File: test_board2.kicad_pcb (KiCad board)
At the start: 2 copper layers, 63.5 x 127 mm, 139 parts, among them P1 MicroB, P2 CONN_01X08, P3 CONN_01X08, P4 CONN_01X10, P5 CONN_01X06, P6 CONN_02X03, Q1 ZXMN2F30FHCT-ND, Q2 Si2305DS, SW1 SWITCH_DPDT, SW2 SW_PUSH, SW3 SW_PUSH, SW4 SW_PUSH, SW5 SW_DIP_8, U1 SM220, U2 AS1115, U3 FT230XS, U4 LD1117S33CTR, U5 LIS3DH, U6 TPS61070, U7 NLSX4373

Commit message: Backup
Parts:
- added ?: MountingHole_3mm, Mounting_Holes:MountingHole_3mm, F.Cu at (203.7, 34.0)
- added ?: MountingHole_3mm, Mounting_Holes:MountingHole_3mm, F.Cu at (146.8, 34.0)
- added ?: MountingHole_3mm, Mounting_Holes:MountingHole_3mm, F.Cu at (175.3, 129.5)
- moved D72 134.4 mm to (179.8, 81.3), turned to 180 degrees
- moved D75 131.8 mm to (179.8, 73.7), turned to 180 degrees
- moved D71 128.5 mm to (179.8, 83.8), turned to 180 degrees
- moved D74 125.7 mm to (179.8, 76.2), turned to 180 degrees
- moved D70 122.8 mm to (179.8, 86.4), turned to 180 degrees
- moved D2 121.7 mm to (179.8, 91.4), turned to 180 degrees
- moved D73 119.7 mm to (179.8, 78.7), turned to 180 degrees
- moved D69 117.3 mm to (179.8, 88.9), turned to 180 degrees
- moved R3 56.5 mm to (162.8, 127.8)
- moved R2 54.3 mm to (163.1, 134.6)
- moved C11 50.6 mm to (156.2, 126.5), turned to 180 degrees
- moved C15 50.6 mm to (163.1, 132.3)
- moved C12 49.7 mm to (156.2, 128.5), turned to 180 degrees
- moved Q2 46.9 mm to (156.5, 122.9), turned to 180 degrees
- moved R5 45.1 mm to (166.1, 139.2), turned to 180 degrees
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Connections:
- C11 pad 1: /VREG_IN -> /VIN_USB
- C12 pad 1: /VREG_IN -> /VIN_USB
- SW5 pad 1: Net-(SW5-Pad1) -> Net-(D75-Pad1)
- SW5 pad 10: Net-(D69-Pad1) -> Net-(SW5-Pad10)
- SW5 pad 11: Net-(D70-Pad1) -> Net-(SW5-Pad10)
- SW5 pad 12: Net-(D71-Pad1) -> Net-(SW5-Pad10)
- SW5 pad 13: Net-(D72-Pad1) -> Net-(SW5-Pad10)
- SW5 pad 14: Net-(D73-Pad1) -> Net-(SW5-Pad10)
- SW5 pad 15: Net-(D74-Pad1) -> Net-(SW5-Pad10)
- SW5 pad 16: Net-(D75-Pad1) -> Net-(SW5-Pad10)
- SW5 pad 2: Net-(SW5-Pad1) -> Net-(D74-Pad1)
- SW5 pad 3: Net-(SW5-Pad1) -> Net-(D73-Pad1)
- SW5 pad 4: Net-(SW5-Pad1) -> Net-(D72-Pad1)
- SW5 pad 5: Net-(SW5-Pad1) -> Net-(D71-Pad1)
- SW5 pad 6: Net-(SW5-Pad1) -> Net-(D70-Pad1)
- SW5 pad 7: Net-(SW5-Pad1) -> Net-(D69-Pad1)
- SW5 pad 8: Net-(SW5-Pad1) -> Net-(D2-Pad1)
- SW5 pad 9: Net-(D2-Pad1) -> Net-(SW5-Pad10)
- U2 pad 12: Net-(SW5-Pad1) -> Net-(SW5-Pad10)
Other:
- board text added: "!! 3V I/O ONLY !!"
- board text added: "A0"
- board text added: "A1"
- board text added: "A2"
- board text added: "A3"
- board text added: "A4"
- board text added: "A5"
- board text added: "D0"
- board text added: "D1"
- board text added: "D10"
- board text added: "D2"
- board text added: "D3"
- board text added: "D4"
- board text added: "D5"
- board text added: "D6"
- board text added: "D7"
- board text added: "D8"
- board text added: "D9"
- board text added: "GND"
- board text added: "ICSP"
- board text added: "MISO"
- board text added: "MOSI"
- board text added: "R"
- board text added: "RST"
- board text added: "Ref"
- board text added: "Reset"
- board text added: "SCK"
- board text added: "SCL"
- board text added: "SDA"
- board text added: "T"
- board text added: "Vcc"
- board text added: "Vin"

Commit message: Placement complete.
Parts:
- added ?: , Synapse:ESC_logo, F.Cu at (153.1, 26.1)
- added Fiducial_Mark: VAL**, Tinkerforge:Fiducial_Mark, F.Cu at (191.5, 145.5)
- added Fiducial_Mark: VAL**, Tinkerforge:Fiducial_Mark, F.Cu at (151.9, 31.8)
- added Fiducial_Mark: VAL**, Tinkerforge:Fiducial_Mark, F.Cu at (198.6, 31.8)
- added R16: 4.7k, Resistors_SMD:R_0603, F.Cu at (157.2, 71.4)
- U7: footprint Housings_SOIC:SOIC-8_3.9x4.9mm_Pitch1.27mm -> Synapse:SOIC-8_3.9x4.9mm_Pitch1.27mm
- moved C13 123.0 mm to (203.5, 70.4), turned to 270 degrees
- moved C22 122.1 mm to (169.4, 71.4), turned to 180 degrees
- moved C23 121.7 mm to (165.9, 71.4), turned to 180 degrees
- moved C14 120.3 mm to (201.2, 70.4), turned to 270 degrees
- moved R15 114.3 mm to (195.6, 95.2), turned to 90 degrees
- moved R14 114.1 mm to (195.6, 98.6), turned to 90 degrees
- moved U7 108.9 mm to (200.7, 56.6), turned to 180 degrees
- moved C7 99.2 mm to (173.0, 71.4)
- moved R10 96.3 mm to (165.9, 95.2), turned to 90 degrees
- moved R7 91.2 mm to (168.4, 95.2), turned to 90 degrees
- moved R8 90.6 mm to (170.9, 95.2), turned to 90 degrees
- moved R6 85.0 mm to (155.7, 98.0), turned to 90 degrees
- moved C9 84.4 mm to (178.8, 96.0), turned to 270 degrees
- moved C10 83.6 mm to (181.1, 96.0), turned to 270 degrees
- moved U5 80.3 mm to (175.3, 96.8), turned to 270 degrees
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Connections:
- U1 pad G1: Net-(U1-PadG1) -> GND
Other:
- net class Default: clearance 0.254 -> 0.2032
- rule trace_clearance: 0.254 -> 0.2032
- board text added: "2016"
- board text removed: "ESC 2016"

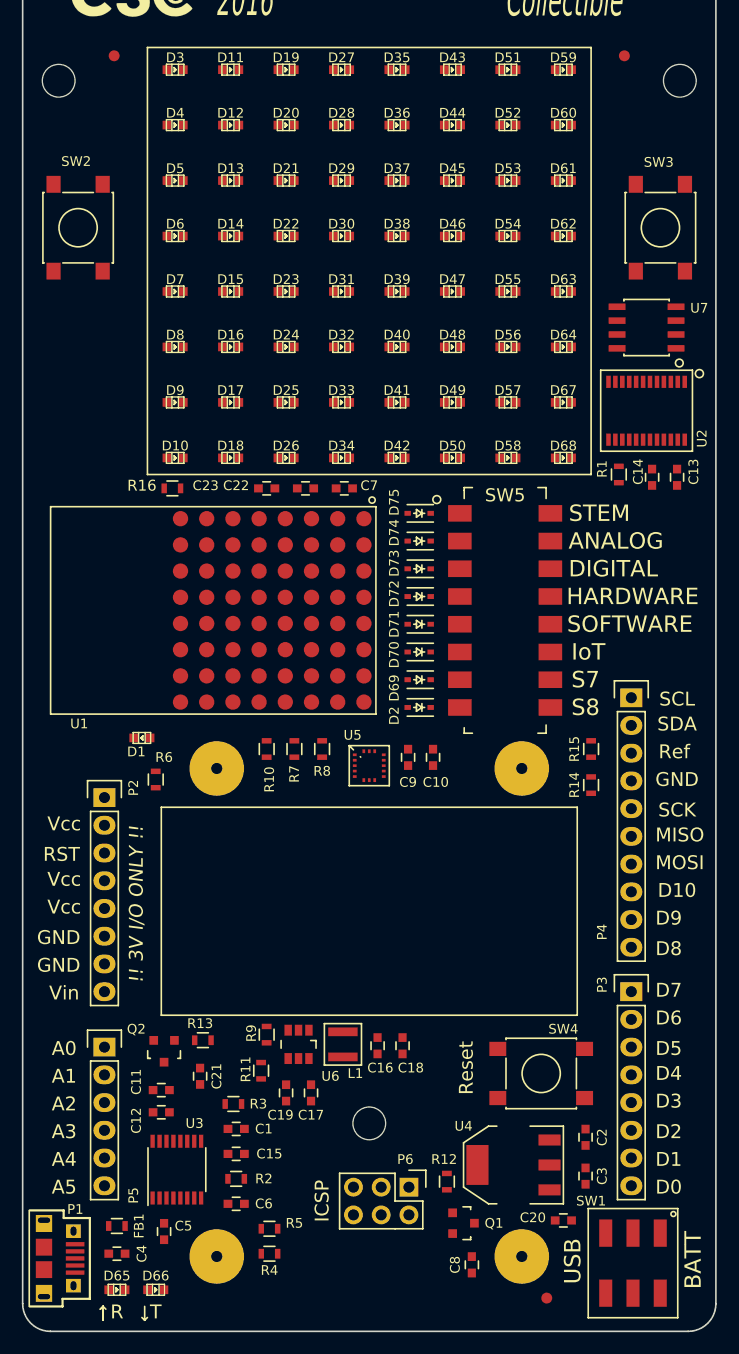
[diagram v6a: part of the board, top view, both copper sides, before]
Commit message: LEDs routed
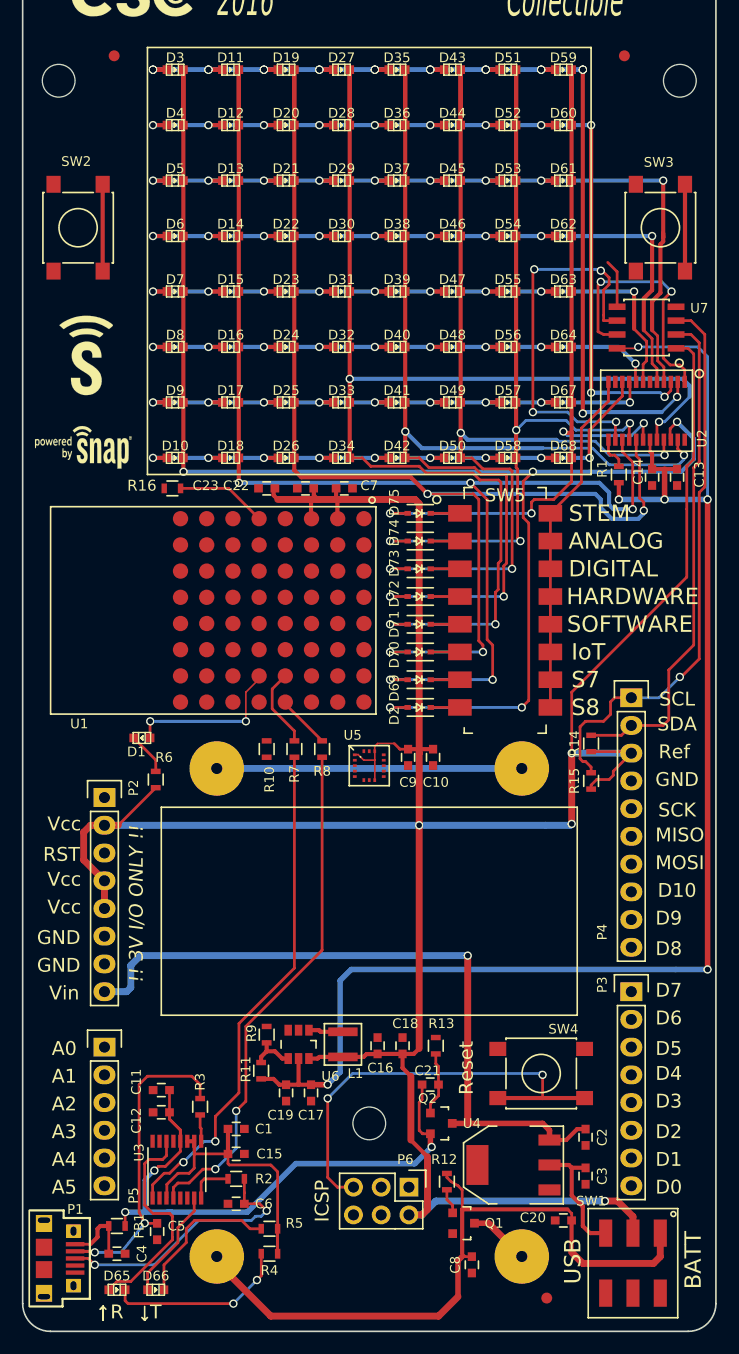
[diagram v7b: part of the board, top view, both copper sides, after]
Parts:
- added ?: , Synapse:pb_snap, F.Cu at (149.1, 67.6)
- added ?: , Synapse:syn_logo1_8x8, F.Cu at (149.4, 59.2)
- moved Q2 26.2 mm to (181.9, 129.5), turned to 270 degrees
- moved R13 21.3 mm to (181.4, 122.4), turned to 270 degrees
- moved C21 21.1 mm to (180.8, 126.0), turned to 0 degrees
- moved R14 3.81 mm to (195.6, 94.7)
- moved R3 3.06 mm to (159.8, 128.0), turned to 90 degrees
- moved R15 2.92 mm to (195.6, 98.2)
- moved C5 0.63 mm to (155.8, 139.4)
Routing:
- net VCC: track 0.00 -> 251.5 mm, vias 0 -> 4
- net /LED_matrix/DIG0: track 0.00 -> 144.0 mm, vias 0 -> 20
- net /LED_matrix/LED_3V: track 0.00 -> 135.1 mm, vias 0 -> 6
- net /LED_matrix/SEGDP: track 0.00 -> 131.2 mm, vias 0 -> 5
- net /LED_matrix/SEGC: track 0.00 -> 117.8 mm, vias 0 -> 4
- net /LED_matrix/SEGA: track 0.00 -> 117.3 mm, vias 0 -> 5
- net /LED_matrix/SEGB: track 0.00 -> 112.5 mm, vias 0 -> 4
- net /LED_matrix/SEGD: track 0.00 -> 102.9 mm, vias 0 -> 4
- net /LED_matrix/SEGE: track 0.00 -> 88.6 mm, vias 0 -> 4
- net /LED_matrix/DIG1: track 0.00 -> 83.4 mm, vias 0 -> 11
- net /LED_matrix/DIG2: track 0.00 -> 76.7 mm, vias 0 -> 9
- net /LED_matrix/SEGF: track 0.00 -> 75.0 mm, vias 0 -> 4
- net /LED_matrix/SEGG: track 0.00 -> 73.2 mm, vias 0 -> 4
- net /LED_matrix/DIG3: track 0.00 -> 70.1 mm, vias 0 -> 9
- net /VREG_IN: track 0.00 -> 65.1 mm, vias 0 -> 1
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
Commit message: Routing complete
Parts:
- moved SW2 53.3 mm to (201.9, 47.5)
- moved SW3 53.3 mm to (148.6, 47.5)
- moved D1 29.2 mm to (183.6, 95.8), turned to 270 degrees
- moved R6 27.2 mm to (182.9, 99.4), turned to 0 degrees
- moved R10 6.04 mm to (171.7, 96.8)
- moved R8 2.16 mm to (169.4, 96.8)
- moved R7 1.98 mm to (167.1, 96.8)
- moved R16 0.25 mm to (157.2, 71.1)
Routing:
- net /BTN_LFT: track 7.95 -> 132.9 mm, vias 0 -> 3
- net /PE0: track 0.00 -> 122.8 mm, vias 0 -> 5
- net /MOSI: track 0.00 -> 121.6 mm, vias 0 -> 4
- net /MISO: track 0.00 -> 117.9 mm, vias 0 -> 4
- net /PE1: track 0.00 -> 117.3 mm, vias 0 -> 5
- net LED_PWR_EN: track 4.42 -> 113.3 mm, vias 0 -> 4
- net /PE4: track 0.00 -> 104.9 mm, vias 0 -> 5
- net /SCLK: track 0.00 -> 100.5 mm, vias 0 -> 3
- net /PB7: track 0.00 -> 91.3 mm, vias 0 -> 5
- net /*IS_USB: track 0.00 -> 91.1 mm, vias 0 -> 4
- net /PE7: track 0.00 -> 82.0 mm, vias 0 -> 3
- net /PF0: track 0.00 -> 78.8 mm, vias 0 -> 1
- net /PF1: track 0.00 -> 77.7 mm, vias 0 -> 1
- net /PF4: track 0.00 -> 76.0 mm, vias 0 -> 1
- net /PF5: track 0.00 -> 75.6 mm, vias 0 -> 1
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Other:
- board text added: "L"
- board text added: "STATUS"
